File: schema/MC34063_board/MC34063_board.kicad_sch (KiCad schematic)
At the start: 9 parts, among them U1 MC34063AP

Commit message: Simulation and updates for smps board
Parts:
- removed D1: 1N5819, Diode_THT:D_DO-41_SOD81_P10.16mm_Horizontal, symbol Diode:1N5819
- added D1: 1N4001, Diode_THT:D_DO-41_SOD81_P10.16mm_Horizontal, symbol Diode:1N4001
- added Rl1: 20, symbol Device:R
- added V1: 12, symbol Simulation_SPICE:VDC
- renumbered C3 to Co1
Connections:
- net GND: now also D1.2 (A), Rl1.2, V1.2
- net at L1.1, U1.2 (SwE): now also D1.1 (K)
- net at Co1.1, L1.2, R2.2: now also Rl1.1
- net +15V renamed VCC
- net VCC: now also V1.1

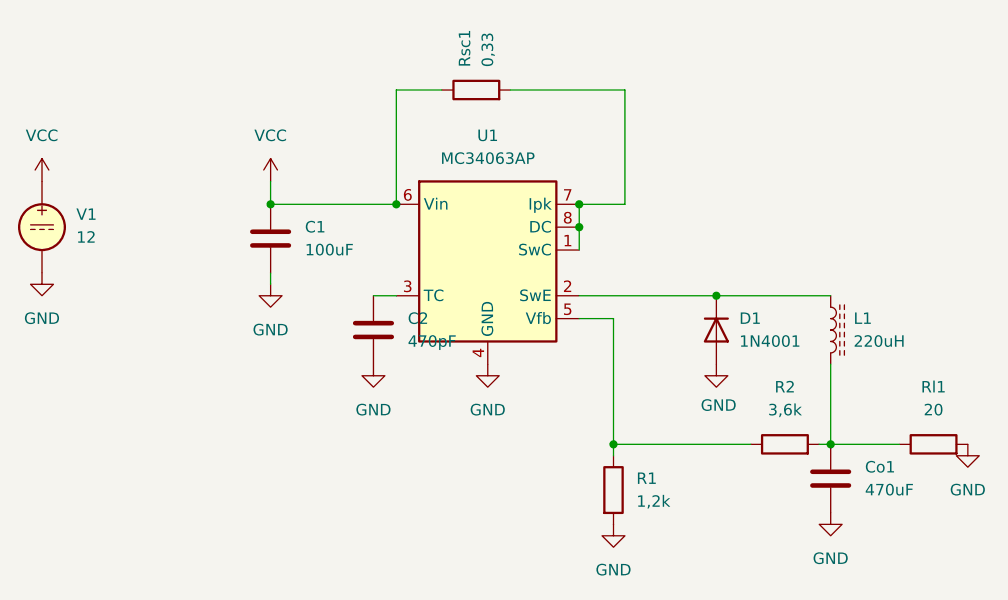
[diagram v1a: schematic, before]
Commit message: Schema updates
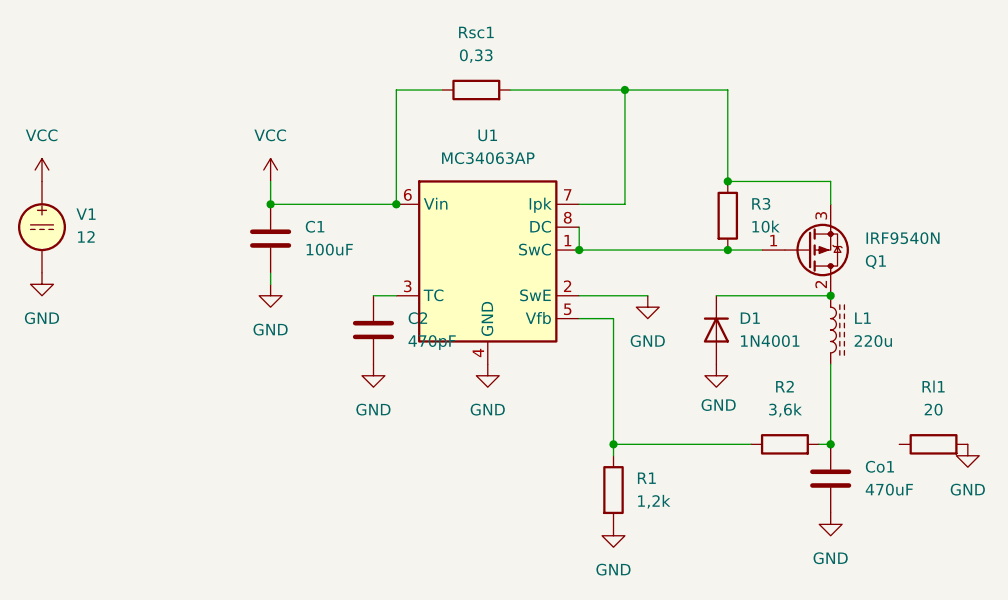
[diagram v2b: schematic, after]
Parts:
- added Q1: IRF9540N, Package_TO_SOT_THT:TO-220-3_Vertical, symbol Transistor_FET:IRF9540N
- added R3: 10k, symbol Device:R
- L1: value 220uH -> 220u
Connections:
- net GND: now also U1.2 (SwE)
- net at Co1.1, L1.2, R2.2: no longer Rl1.1
- net at U1.1 (SwC), U1.8 (DC): now also Q1.1 (G), R3.2; no longer Rsc1.2, U1.7 (Ipk)
- net at D1.1 (K), L1.1: now also Q1.2 (D); no longer U1.2 (SwE)
- new net: Q1.3 (S), R3.1, Rsc1.2, U1.7 (Ipk)

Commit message: Various 3D models and such
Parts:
- removed L1: 220u, Inductor_SMD:L_Pulse_PA4332, symbol Device:L_Ferrite
- added L1: 330uH, symbol Device:L
- added R5, R6: 1M, symbol Device:R
- Co1: value 470uF -> 200uf
- Rsc1: value 0,33 -> 0,1
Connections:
- net GND: now also R5.2, R6.2
- net VCC: now also U1.8 (DC), R5.1
- net at Q1.1 (G), R3.2, U1.1 (SwC): no longer U1.8 (DC)
- net at D1.1 (K), Q1.2 (D): now also L1.1
- net at C2.1, U1.3 (TC): now also R6.1
- net at Co1.1, R2.2: now also Rl1.1, L1.2
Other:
- moved on the sheet: D1, R3
